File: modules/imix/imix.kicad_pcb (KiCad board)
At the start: 2 copper layers, 30.5 x 68.6 mm, 35 parts, among them U1 MCP6002-xSN, U2 MCP6002-xSN, U3 MCP6002-xSN

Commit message: imix_1.0.0
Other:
- board text added: "IMIX 1.0.0"
- board text removed: "IMIX 0.2.0"
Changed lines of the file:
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@@
 		)
 	)
-	(gr_text "IMIX\n0.2.0"
+	(gr_text "IMIX\n1.0.0"
 		(at 76.327 107.95 0)
 		(layer "F.SilkS")

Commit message: Add improved schematics
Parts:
- removed C1, C2, C4: 0.1uf, Capacitor_SMD:C_0402_1005Metric
- removed C3: 100uf, Capacitor_SMD:C_1206_3216Metric
- removed R1, R12, R2: 1k, Resistor_SMD:R_0402_1005Metric
- removed R10, R11, R4, R6, R8: 200k, Resistor_SMD:R_0402_1005Metric
- removed R13, R14, R15, R16, R17, R18, R19, R20: 100k, Resistor_SMD:R_0402_1005Metric
- removed R3, R5, R7, R9: 1M, Resistor_SMD:R_0402_1005Metric
- removed RV1, RV2, RV3, RV4: 50k, BreadModular_Pots:Potentiometer_RV09
- removed U1, U2, U3: MCP6002-xSN, Package_SO:SOIC-8-1EP_3.9x4.9mm_P1.27mm_EP2.29x3mm
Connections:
- INPUT1 pad 1: IN_1 -> unconnected-(INPUT1-Pin_1-Pad1)
- INPUT1 pad 2: IN_2 -> unconnected-(INPUT1-Pin_2-Pad2)
- INPUT1 pad 3: IN_3 -> unconnected-(INPUT1-Pin_3-Pad3)
- INPUT1 pad 4: IN_4 -> unconnected-(INPUT1-Pin_4-Pad4)
- OUTPUT1 pad 1: MIXOUT -> unconnected-(OUTPUT1-Pin_1-Pad1)
- OUTPUT1 pad 2: MIXOUT -> unconnected-(OUTPUT1-Pin_2-Pad2)
- OUTPUT1 pad 3: MIXOUT -> unconnected-(OUTPUT1-Pin_3-Pad3)
- OUTPUT1 pad 4: MIXOUT -> unconnected-(OUTPUT1-Pin_4-Pad4)
- OUTPUT1 pad 5: MIXOUT -> unconnected-(OUTPUT1-Pin_5-Pad5)
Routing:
- net V_MID: track 256.7 -> 0.00 mm, vias 9 -> 0
- net GND: track 160.5 -> 10.2 mm, vias 6 -> 0
- net V_SUPPLY: track 109.3 -> 10.2 mm, vias 5 -> 0
- net IN_4: track 51.0 -> 0.00 mm, vias 4 -> 0
- net MIXOUT: track 50.9 -> 0.00 mm
- net Net-(R17-Pad2): track 48.7 -> 0.00 mm, vias 2 -> 0
- net Net-(R19-Pad2): track 38.4 -> 0.00 mm, vias 2 -> 0
- net IN_3: track 38.1 -> 0.00 mm, vias 1 -> 0
- net Net-(U3A--): track 33.7 -> 0.00 mm
- net Net-(R13-Pad2): track 29.7 -> 0.00 mm, vias 4 -> 0
- net Net-(R15-Pad2): track 24.2 -> 0.00 mm, vias 2 -> 0
- net IN_2: track 22.5 -> 0.00 mm
- net IN_1: track 21.7 -> 0.00 mm, vias 2 -> 0
- net Net-(U2A--): track 20.5 -> 0.00 mm, vias 2 -> 0
- net Net-(U1B--): track 20.4 -> 0.00 mm, vias 4 -> 0
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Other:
- board text added: "NAME"
- board text added: "NAME 0.0.0"
- board text removed: "1"
- board text removed: "2"
- board text removed: "3"
- board text removed: "4"
- board text removed: "IMIX"
- board text removed: "IMIX 1.0.0"
- board text removed: "MIXOUT"

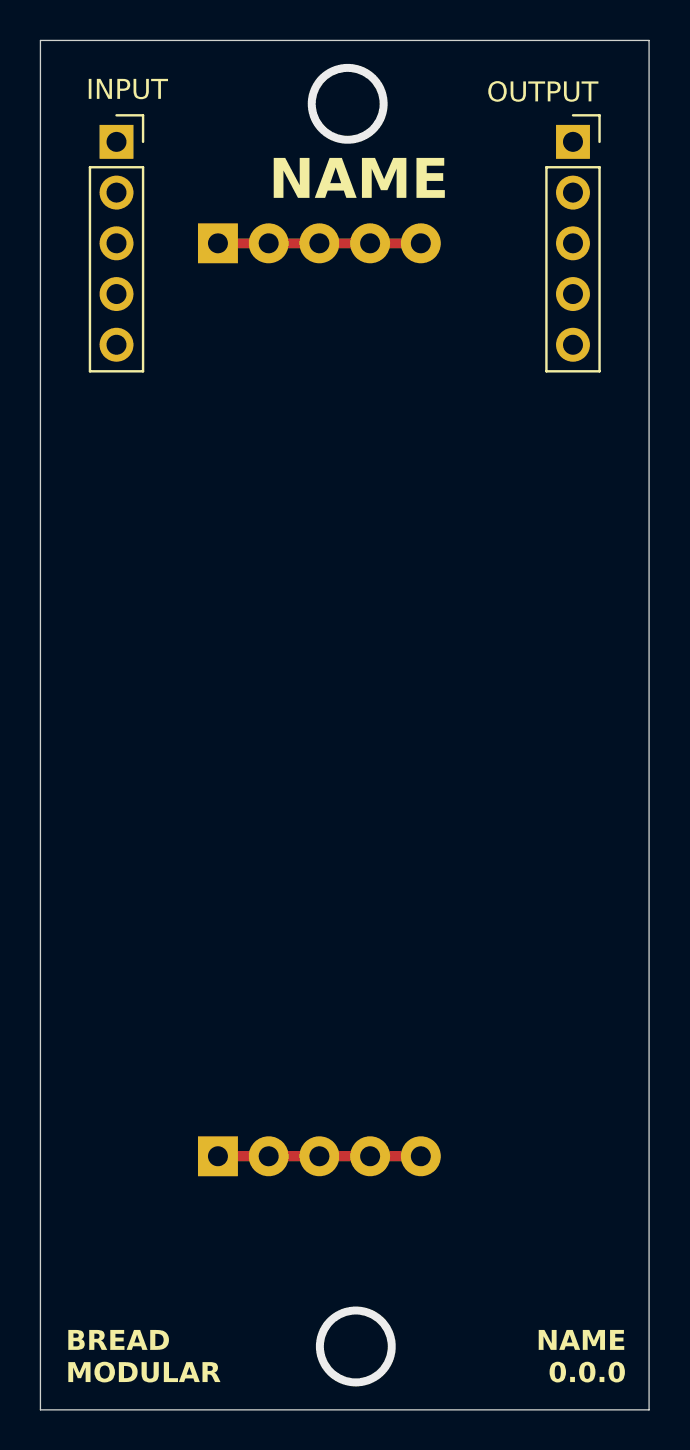
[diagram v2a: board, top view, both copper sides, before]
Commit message: Add the initial revered board for layout
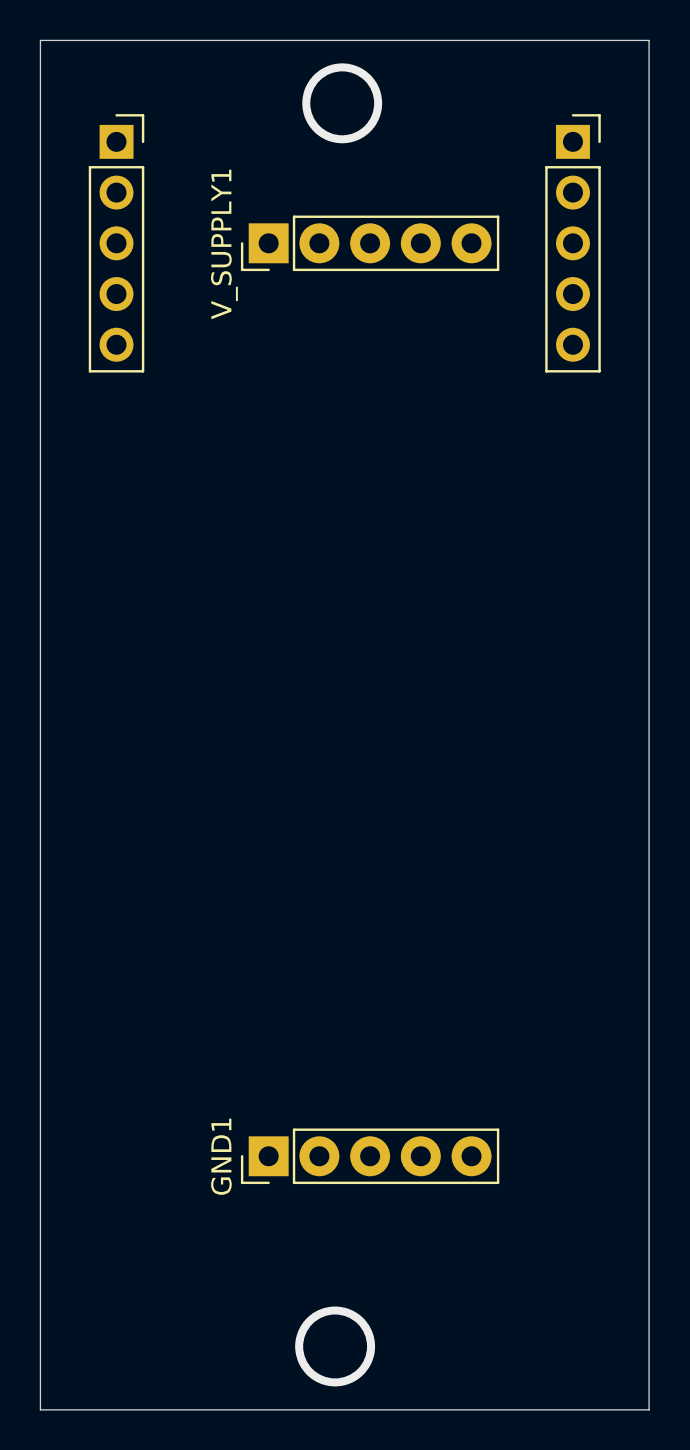
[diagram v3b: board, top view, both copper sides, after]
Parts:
- GND1, V_SUPPLY1: moved to F.Cu
- moved INPUT1 22.9 mm to (73.7, 45.7)
- moved OUTPUT1 22.9 mm to (50.8, 45.7)
- moved GND1 2.54 mm to (58.4, 96.5), turned to 90 degrees
- moved V_SUPPLY1 2.54 mm to (58.4, 50.8), turned to 90 degrees
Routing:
- net V_SUPPLY: track 10.2 -> 0.00 mm
- net GND: track 10.2 -> 0.00 mm
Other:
- board text added: "IMIX"
- board text added: "IMIX 1.5.0"
- board text removed: "NAME"
- board text removed: "NAME 0.0.0"

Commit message: Start placing the PCB
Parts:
- added C1: 100pf, Capacitor_SMD:C_0402_1005Metric, F.Cu at (147.9, 52.4)
- added C10: 0.1uf, Capacitor_SMD:C_0402_1005Metric, F.Cu at (150.7, 58.3)
- added C11: 0.1uf, Capacitor_SMD:C_0402_1005Metric, F.Cu at (150.7, 60.2)
- added C12: 0.1uf, Capacitor_SMD:C_0402_1005Metric, F.Cu at (150.7, 62.2)
- added C13: 100pf, Capacitor_SMD:C_0402_1005Metric, F.Cu at (153.6, 52.4)
- added C14: 0.1uf, Capacitor_SMD:C_0402_1005Metric, F.Cu at (153.6, 54.3)
- added C15: 0.1uf, Capacitor_SMD:C_0402_1005Metric, F.Cu at (54.0, 58.5)
- added C16: 100uf, Capacitor_SMD:C_1206_3216Metric, F.Cu at (54.0, 55.4)
- added C17: 0.1uf, Capacitor_SMD:C_0402_1005Metric, F.Cu at (153.6, 58.3)
- added C18: 0.1uf, Capacitor_SMD:C_0402_1005Metric, F.Cu at (153.6, 60.2)
- added C2: 100pf, Capacitor_SMD:C_0402_1005Metric, F.Cu at (147.9, 54.3)
- added C3: 100pf, Capacitor_SMD:C_0402_1005Metric, F.Cu at (147.9, 56.3)
- added C4: 100pf, Capacitor_SMD:C_0402_1005Metric, F.Cu at (147.9, 58.3)
- added C5: 10uf, Capacitor_SMD:C_0402_1005Metric, F.Cu at (147.9, 60.2)
- added C6: 10uf, Capacitor_SMD:C_0402_1005Metric, F.Cu at (147.9, 62.2)
- added C7: 0.1uf, Capacitor_SMD:C_0402_1005Metric, F.Cu at (150.7, 52.4)
- added C8: 10uf, Capacitor_SMD:C_0402_1005Metric, F.Cu at (150.7, 54.3)
- added C9: 10uf, Capacitor_SMD:C_0402_1005Metric, F.Cu at (150.7, 56.3)
- added R1: 1M, Resistor_SMD:R_0402_1005Metric, F.Cu at (136.3, 52.4)
- added R10: 22k, Resistor_SMD:R_0402_1005Metric, F.Cu at (139.2, 54.4)
- added R11: 22k, Resistor_SMD:R_0402_1005Metric, F.Cu at (139.2, 56.4)
- added R12: 22k, Resistor_SMD:R_0402_1005Metric, F.Cu at (139.2, 58.3)
- added R13: 100, Resistor_SMD:R_0402_1005Metric, F.Cu at (139.2, 60.3)
- added R14: 100, Resistor_SMD:R_0402_1005Metric, F.Cu at (139.2, 62.3)
- added R15: 100, Resistor_SMD:R_0402_1005Metric, F.Cu at (139.2, 64.3)
- added R16: 100, Resistor_SMD:R_0402_1005Metric, F.Cu at (139.2, 66.3)
- added R17: 22k, Resistor_SMD:R_0402_1005Metric, F.Cu at (142.1, 52.4)
- added R18: 22k, Resistor_SMD:R_0402_1005Metric, F.Cu at (142.1, 54.4)
- added R19: 22k, Resistor_SMD:R_0402_1005Metric, F.Cu at (142.1, 56.4)
- added R2: 1M, Resistor_SMD:R_0402_1005Metric, F.Cu at (136.3, 54.4)
- added R20: 22k, Resistor_SMD:R_0402_1005Metric, F.Cu at (142.1, 58.3)
- added R21: 100, Resistor_SMD:R_0402_1005Metric, F.Cu at (142.1, 60.3)
- added R22: 100, Resistor_SMD:R_0402_1005Metric, F.Cu at (142.1, 62.3)
- added R23: 100, Resistor_SMD:R_0402_1005Metric, F.Cu at (142.1, 64.3)
- added R24: 100, Resistor_SMD:R_0402_1005Metric, F.Cu at (142.1, 66.3)
- added R25: 22k, Resistor_SMD:R_0402_1005Metric, F.Cu at (145.0, 52.4)
- added R26: 1k, Resistor_SMD:R_0402_1005Metric, F.Cu at (145.0, 54.4)
- added R27: 10k, Resistor_SMD:R_0402_1005Metric, F.Cu at (56.7, 54.8)
- added R28: 10k, Resistor_SMD:R_0402_1005Metric, F.Cu at (56.7, 57.1)
- added R29: 10, Resistor_SMD:R_0402_1005Metric, F.Cu at (56.7, 58.5)
- added R3: 1M, Resistor_SMD:R_0402_1005Metric, F.Cu at (136.3, 56.4)
- added R4: 1M, Resistor_SMD:R_0402_1005Metric, F.Cu at (136.3, 58.3)
- added R5: 22k, Resistor_SMD:R_0402_1005Metric, F.Cu at (136.3, 60.3)
- added R6: 22k, Resistor_SMD:R_0402_1005Metric, F.Cu at (136.3, 62.3)
- added R7: 22k, Resistor_SMD:R_0402_1005Metric, F.Cu at (136.3, 64.3)
- added R8: 22k, Resistor_SMD:R_0402_1005Metric, F.Cu at (136.3, 66.3)
- added R9: 22k, Resistor_SMD:R_0402_1005Metric, F.Cu at (139.2, 52.4)
- added RV1: 50k, BreadModular_Pots:Potentiometer_RV09, B.Cu at (69.8, 64.0)
- added RV2: 50k, BreadModular_Pots:Potentiometer_RV09, B.Cu at (54.6, 64.0)
- added RV3: 50k, BreadModular_Pots:Potentiometer_RV09, B.Cu at (69.8, 92.7)
- added RV4: 50k, BreadModular_Pots:Potentiometer_RV09, B.Cu at (54.6, 92.7)
- added U1: MCP6002-xSN, Package_SO:SOIC-8-1EP_3.9x4.9mm_P1.27mm_EP2.29x3mm, F.Cu at (70.0, 79.3)
- added U2: MCP6002-xSN, Package_SO:SOIC-8-1EP_3.9x4.9mm_P1.27mm_EP2.29x3mm, F.Cu at (54.3, 79.3)
- added U3: MCP6002-xSN, Package_SO:SOIC-8-1EP_3.9x4.9mm_P1.27mm_EP2.29x3mm, F.Cu at (62.6, 57.2)
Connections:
- INPUT1 pad 1: unconnected-(INPUT1-Pin_1-Pad1) -> IN_1
- INPUT1 pad 2: unconnected-(INPUT1-Pin_2-Pad2) -> IN_2
- INPUT1 pad 3: unconnected-(INPUT1-Pin_3-Pad3) -> IN_3
- INPUT1 pad 4: unconnected-(INPUT1-Pin_4-Pad4) -> IN_4
- OUTPUT1 pad 1: unconnected-(OUTPUT1-Pin_1-Pad1) -> MIXOUT
- OUTPUT1 pad 2: unconnected-(OUTPUT1-Pin_2-Pad2) -> MIXOUT
- OUTPUT1 pad 3: unconnected-(OUTPUT1-Pin_3-Pad3) -> MIXOUT
- OUTPUT1 pad 4: unconnected-(OUTPUT1-Pin_4-Pad4) -> MIXOUT
- OUTPUT1 pad 5: unconnected-(OUTPUT1-Pin_5-Pad5) -> MIXOUT
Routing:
- net Net-(U3B-+): track 0.00 -> 9.89 mm
- net Net-(U3B--): track 0.00 -> 4.48 mm
- net GND: track 0.00 -> 3.71 mm, vias 0 -> 4
- net V_SUPPLY: track 0.00 -> 2.58 mm, vias 0 -> 2
- added copper zone on In1.Cu, net GND
- added copper zone on In2.Cu, net V_SUPPLY
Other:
- copper layers 2 -> 4
- board text added: "1"
- board text added: "2"
- board text added: "3"
- board text added: "4"
- board text added: "MIXOUT"

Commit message: Finalized routing
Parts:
- moved C8 104.5 mm to (54.5, 94.9)
- moved C14 103.7 mm to (53.8, 82.7)
- moved C11 103.2 mm to (54.5, 97.4)
- moved C4 101.1 mm to (49.4, 81.2)
- moved R18 100.6 mm to (51.3, 97.7), turned to 180 degrees
- moved C10 94.5 mm to (56.7, 67.4)
- moved C18 92.9 mm to (60.7, 60.9)
- moved R12 92.4 mm to (49.3, 80.0)
- moved R23 92.1 mm to (54.4, 92.4)
- moved C3 92.0 mm to (59.3, 81.3)
- moved C6 91.4 mm to (56.7, 68.7)
- moved R16 91.3 mm to (49.3, 82.6)
- moved R20 90.1 mm to (52.6, 68.4), turned to 180 degrees
- moved R3 89.3 mm to (49.4, 77.4), turned to 180 degrees
- moved R7 88.0 mm to (49.4, 78.7)
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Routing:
- net V_MID: track 0.00 -> 128.5 mm, vias 0 -> 6
- net Net-(U3A--): track 0.00 -> 125.7 mm, vias 0 -> 5
- net V_MID_4: track 0.00 -> 65.3 mm, vias 0 -> 1
- net IN_2: track 0.00 -> 58.3 mm
- net IN_1: track 0.00 -> 38.7 mm
- net IN_4: track 0.00 -> 36.5 mm
- net V_MID_3: track 0.00 -> 35.6 mm, vias 0 -> 1
- net IN_3: track 0.00 -> 31.8 mm
- net MIXOUT: track 0.00 -> 29.0 mm
- net Net-(R14-Pad2): track 0.00 -> 28.5 mm
- net V_MID_1: track 0.00 -> 25.5 mm, vias 0 -> 1
- net Net-(R13-Pad2): track 0.00 -> 20.7 mm
- net V_MID_2: track 0.00 -> 17.8 mm, vias 0 -> 1
- net Net-(R15-Pad2): track 0.00 -> 16.0 mm
- net Net-(R16-Pad2): track 0.00 -> 15.6 mm
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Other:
- board text added: "IMIX 2.0.0"
- board text removed: "IMIX 1.5.0"
